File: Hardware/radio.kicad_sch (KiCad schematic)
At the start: 4 parts, among them J11 Conn_Coaxial, U21 RFM95W-868S2

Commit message: Adding some 3d models
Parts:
- U21: footprint RF_Module:HOPERF_RFM9XW_SMD -> iclr:HOPERF_RFM9XW_SMD
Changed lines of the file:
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@@
 		(shape output)
 		(at 151.13 107.315 0)
-		(fields_autoplaced yes)
 		(effects
 			(font
@@
 		(shape input)
 		(at 125.73 92.075 180)
-		(fields_autoplaced yes)
 		(effects
 			(font
@@
 		(shape output)
 		(at 125.73 94.615 180)
-		(fields_autoplaced yes)
 		(effects
 			(font
@@
 		(shape input)
 		(at 125.73 102.235 180)
-		(fields_autoplaced yes)
 		(effects
 			(font
@@
 		(shape input)
 		(at 125.73 97.155 180)
-		(fields_autoplaced yes)
 		(effects
 			(font
@@
 		(shape input)
 		(at 125.73 89.535 180)
-		(fields_autoplaced yes)
 		(effects
 			(font
@@
 			)
 		)
-		(property "Footprint" "RF_Module:HOPERF_RFM9XW_SMD"
+		(property "Footprint" "iclr:HOPERF_RFM9XW_SMD"
 			(at 54.61 55.245 0)
 			(effects

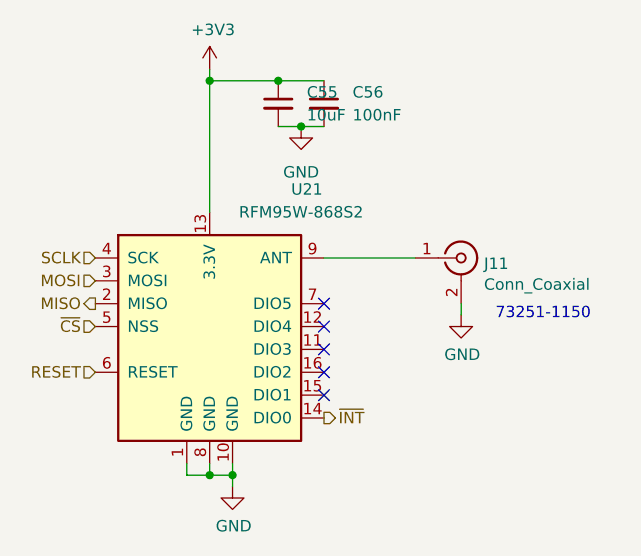
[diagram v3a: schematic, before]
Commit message: cleaned up schematic and bom
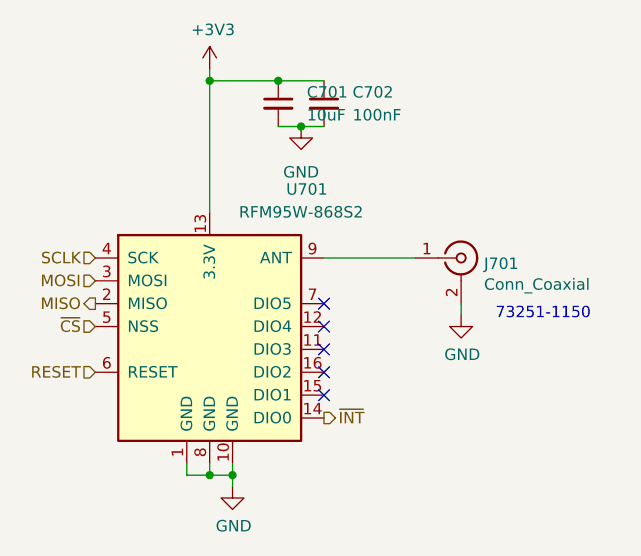
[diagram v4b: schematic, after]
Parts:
- renumbered C55 to C701, C56 to C702, J11 to J701, U21 to U701
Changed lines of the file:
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@@
 (kicad_sch
-	(version 20231120)
+	(version 20250114)
 	(generator "eeschema")
-	(generator_version "8.0")
+	(generator_version "9.0")
 	(paper "A4")
+	(text "73251-1150"
+		(exclude_from_sim no)
+		(at 170.18 96.52 0)
+		(effects
+			(font
+				(size 1.27 1.27)
+			)
+			(justify left bottom)
+		)
+	)
 	(junction
 		(at 140.97 113.665)
@@
 			(width 0)
 			(type default)
-		)
-	)
-	(text "73251-1150"
-		(exclude_from_sim no)
-		(at 170.18 96.52 0)
-		(effects
-			(font
-				(size 1.27 1.27)
-			)
-			(justify left bottom)
 		)
 	)
@@
 		(dnp no)
 		(fields_autoplaced yes)
-		(property "Reference" "C55"
+		(property "Reference" "C701"
 			(at 149.225 71.1262 0)
 			(effects
@@
 			(project "PickleRick"
 				(path "/e63e39d7-6ac0-4ffd-8aa3-1841a4541b55/a5e505c0-c0af-4f61-a9d4-cf031c548012"
-					(reference "C55")
+					(reference "C701")
 					(unit 1)
 				)
@@
 		(on_board yes)
 		(dnp no)
-		(property "Reference" "#PWR0129"
+		(property "Reference" "#PWR0704"
 			(at 166.37 102.235 0)
 			(effects
@@
 			(project "PickleRick"
 				(path "/e63e39d7-6ac0-4ffd-8aa3-1841a4541b55/a5e505c0-c0af-4f61-a9d4-cf031c548012"
-					(reference "#PWR0129")
+					(reference "#PWR0704")
 					(unit 1)
 				)
@@
 		(on_board yes)
 		(dnp no)
-		(property "Reference" "U21"
+		(property "Reference" "U701"
 			(at 149.225 81.915 0)
 			(effects
@@
 			(project "PickleRick"
 				(path "/e63e39d7-6ac0-4ffd-8aa3-1841a4541b55/a5e505c0-c0af-4f61-a9d4-cf031c548012"
-					(reference "U21")
+					(reference "U701")
 					(unit 1)
 				)
@@
 		(on_board yes)
 		(dnp no)
-		(property "Reference" "J11"
+		(property "Reference" "J701"
 			(at 168.91 90.17 0)
 			(effects
@@
 			)
 		)
-		(property "Datasheet" " ~"
+		(property "Datasheet" "~"
 			(at 166.37 89.535 0)
 			(effects
@@
 			(project "PickleRick"
 				(path "/e63e39d7-6ac0-4ffd-8aa3-1841a4541b55/a5e505c0-c0af-4f61-a9d4-cf031c548012"
-					(reference "J11")
+					(reference "J701")
 					(unit 1)
 				)
@@
 		(on_board yes)
 		(dnp no)
-		(property "Reference" "C56"
+		(property "Reference" "C702"
 			(at 154.305 71.1262 0)
 			(effects
@@
 			(project "PickleRick"
 				(path "/e63e39d7-6ac0-4ffd-8aa3-1841a4541b55/a5e505c0-c0af-4f61-a9d4-cf031c548012"
-					(reference "C56")
+					(reference "C702")
 					(unit 1)
 				)
@@
 		(dnp no)
 		(fields_autoplaced yes)
-		(property "Reference" "#PWR0128"
+		(property "Reference" "#PWR0703"
 			(at 148.59 81.28 0)
 			(effects
@@
 			(project "PickleRick"
 				(path "/e63e39d7-6ac0-4ffd-8aa3-1841a4541b55/a5e505c0-c0af-4f61-a9d4-cf031c548012"
-					(reference "#PWR0128")
+					(reference "#PWR0703")
 					(unit 1)
 				)
@@
 		(on_board yes)
 		(dnp no)
-		(property "Reference" "#PWR0126"
+		(property "Reference" "#PWR0701"
 			(at 138.43 72.39 0)
 			(effects
@@
 			(project "PickleRick"
 				(path "/e63e39d7-6ac0-4ffd-8aa3-1841a4541b55/a5e505c0-c0af-4f61-a9d4-cf031c548012"
-					(reference "#PWR0126")
+					(reference "#PWR0701")
 					(unit 1)
 				)
@@
 		(on_board yes)
 		(dnp no)
-		(property "Reference" "#PWR0127"
+		(property "Reference" "#PWR0702"
 			(at 140.97 121.285 0)
 			(effects
@@
 			(project "PickleRick"
 				(path "/e63e39d7-6ac0-4ffd-8aa3-1841a4541b55/a5e505c0-c0af-4f61-a9d4-cf031c548012"
-					(reference "#PWR0127")
+					(reference "#PWR0702")
 					(unit 1)
 				)
